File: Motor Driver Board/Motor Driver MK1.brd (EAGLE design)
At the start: 100 x 80 mm, 82 parts, among them IC1 REG1117

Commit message: Day 2. Everything is lines. How much further can this go?
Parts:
- added AC3: (no value), rcl:C0805
- added LED2: (no value), led:CHIP-LED0805
- added RLED1: 330, resistor:R0805
- moved IC1 38.2 mm to (58.4, 69.8)
- moved FAULT_OUT 5.24 mm to (82.5, 64.8)
- moved FAULT_UP 5.24 mm to (77.5, 64.8)
- moved LED1 3.86 mm to (55.9, 61.6), turned to 90 degrees
- moved RLED 3.17 mm to (61.0, 61.6), turned to 0 degrees
- moved DB 2.84 mm to (27.9, 66.0)
- moved EN_IN 1.27 mm to (73.7, 73.7)
- moved EN_UP 1.27 mm to (72.4, 64.8)
- moved FAULT_IN 1.27 mm to (78.7, 73.7)
- moved ADIR_IN 1.27 mm to (7.62, 57.1)
- moved ADIR_UP 1.27 mm to (6.35, 48.3)
- moved AHOME_IN 1.27 mm to (17.8, 57.1)
- moved AHOME_OUT 1.27 mm to (21.6, 48.3)
- moved AHOME_UP 1.27 mm to (16.5, 48.3)
- moved ASTP_IN 1.27 mm to (12.7, 57.1)
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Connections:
- new net N$31: LED2.A, RLED1.2
- net GND: now also AC3.2, LED2.C
- net VCC: now also AC3.1, RLED1.1
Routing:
- net V+: track 142.5 -> 260.7 mm
- net VCC: track 381.8 -> 437.2 mm, vias 2 -> 3
- net N$31: track 43.2 -> 0.00 mm
- net N$85: track 0.00 -> 30.8 mm
- net N$86: track 0.00 -> 25.4 mm
- net GND: track 115.4 -> 131.8 mm
- net DGND: track 185.7 -> 201.7 mm, vias 0 -> 1
- net N$89: track 0.00 -> 9.73 mm
- net N$76: track 0.00 -> 7.59 mm
- net N$63: track 14.7 -> 21.2 mm, vias 2 -> 1
- net N$82: track 0.00 -> 6.32 mm
- net N$33: track 109.7 -> 115.9 mm
- net N$56: track 181.8 -> 187.2 mm, vias 1 -> 0
- net N$55: track 80.5 -> 75.0 mm, vias 2 -> 1
- net N$88: track 0.00 -> 4.26 mm
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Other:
- board text added: "A"
- board text added: "X"
- board text added: "Y"
- board text added: "Z"

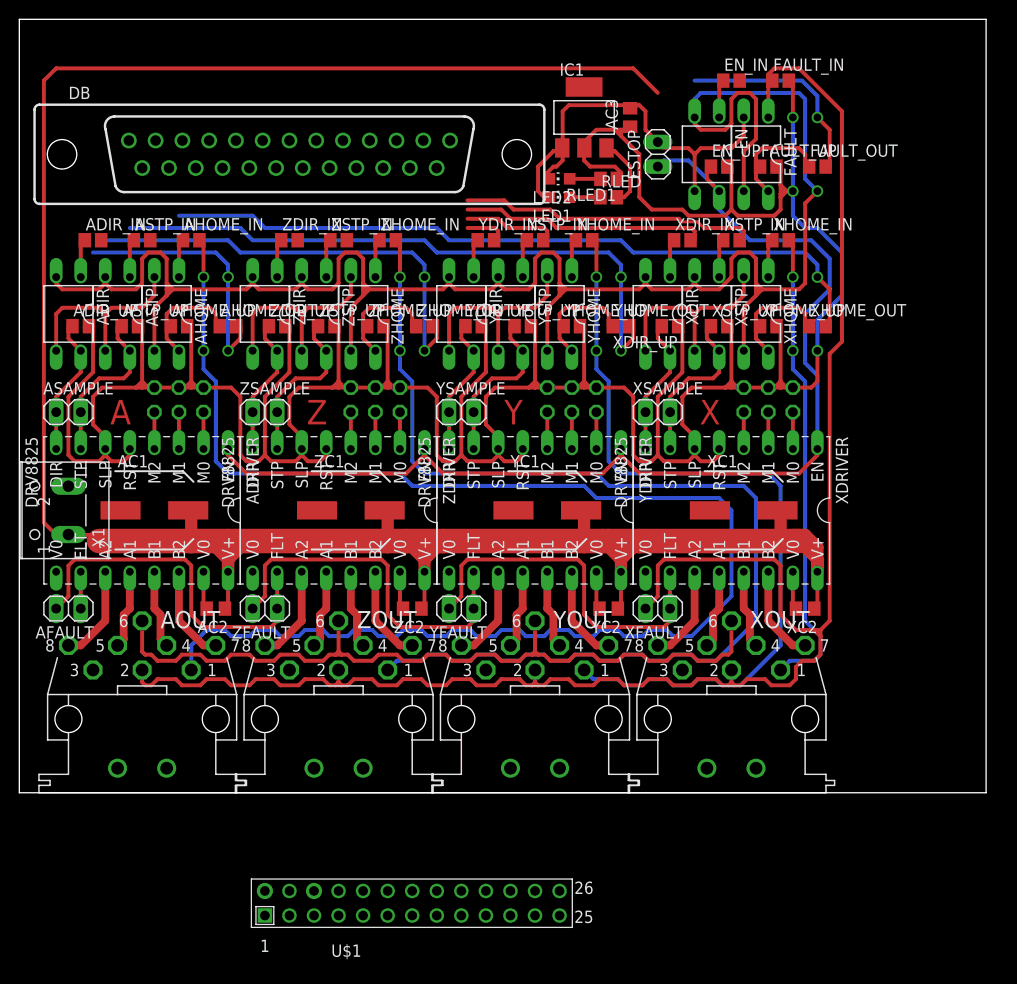
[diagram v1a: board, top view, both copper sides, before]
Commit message: added ground plane, 90% finished.
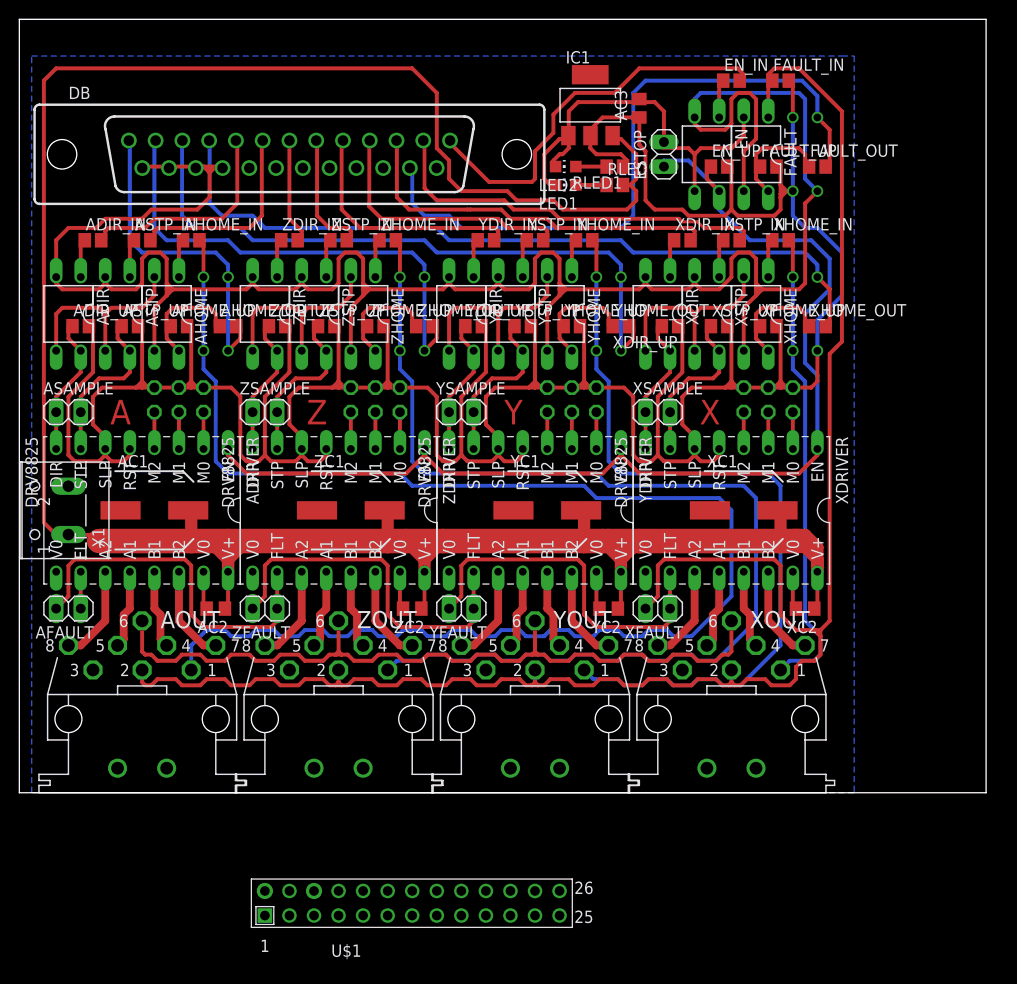
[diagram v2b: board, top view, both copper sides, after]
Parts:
- moved IC1 1.42 mm to (59.1, 71.1)
- moved LED1 1.42 mm to (56.5, 62.9)
- moved RLED 1.42 mm to (61.6, 62.9)
- moved LED2 1.42 mm to (56.5, 64.8)
- moved RLED1 1.42 mm to (61.6, 64.8)
- moved AC3 1.35 mm to (64.1, 70.8)
- moved ESTOP 0.63 mm to (66.7, 66.0)
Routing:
- net N$59: track 0.00 -> 69.0 mm, vias 0 -> 1
- net N$52: track 0.00 -> 40.6 mm
- net N$54: track 0.00 -> 40.1 mm
- net N$51: track 0.00 -> 38.9 mm
- net DGND: track 201.7 -> 236.4 mm
- net N$85: track 30.8 -> 0.00 mm
- net N$49: track 0.00 -> 27.4 mm
- net N$86: track 25.4 -> 0.00 mm
- net N$48: track 0.00 -> 25.4 mm
- net N$42: track 0.00 -> 22.3 mm
- net N$63: track 21.2 -> 0.00 mm, vias 1 -> 0
- net N$43: track 0.00 -> 20.7 mm
- net V+: track 260.7 -> 277.7 mm
- net N$45: track 0.00 -> 12.7 mm
- net N$44: track 0.00 -> 10.7 mm
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- added copper zone on layer 16, net GND
